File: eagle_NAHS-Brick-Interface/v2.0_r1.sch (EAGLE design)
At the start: 8 parts, among them IC1 FT232RL, J1 NAHS-BRICK-INTERFACE-V2_I-SIDE, J2 10118194-0001LF

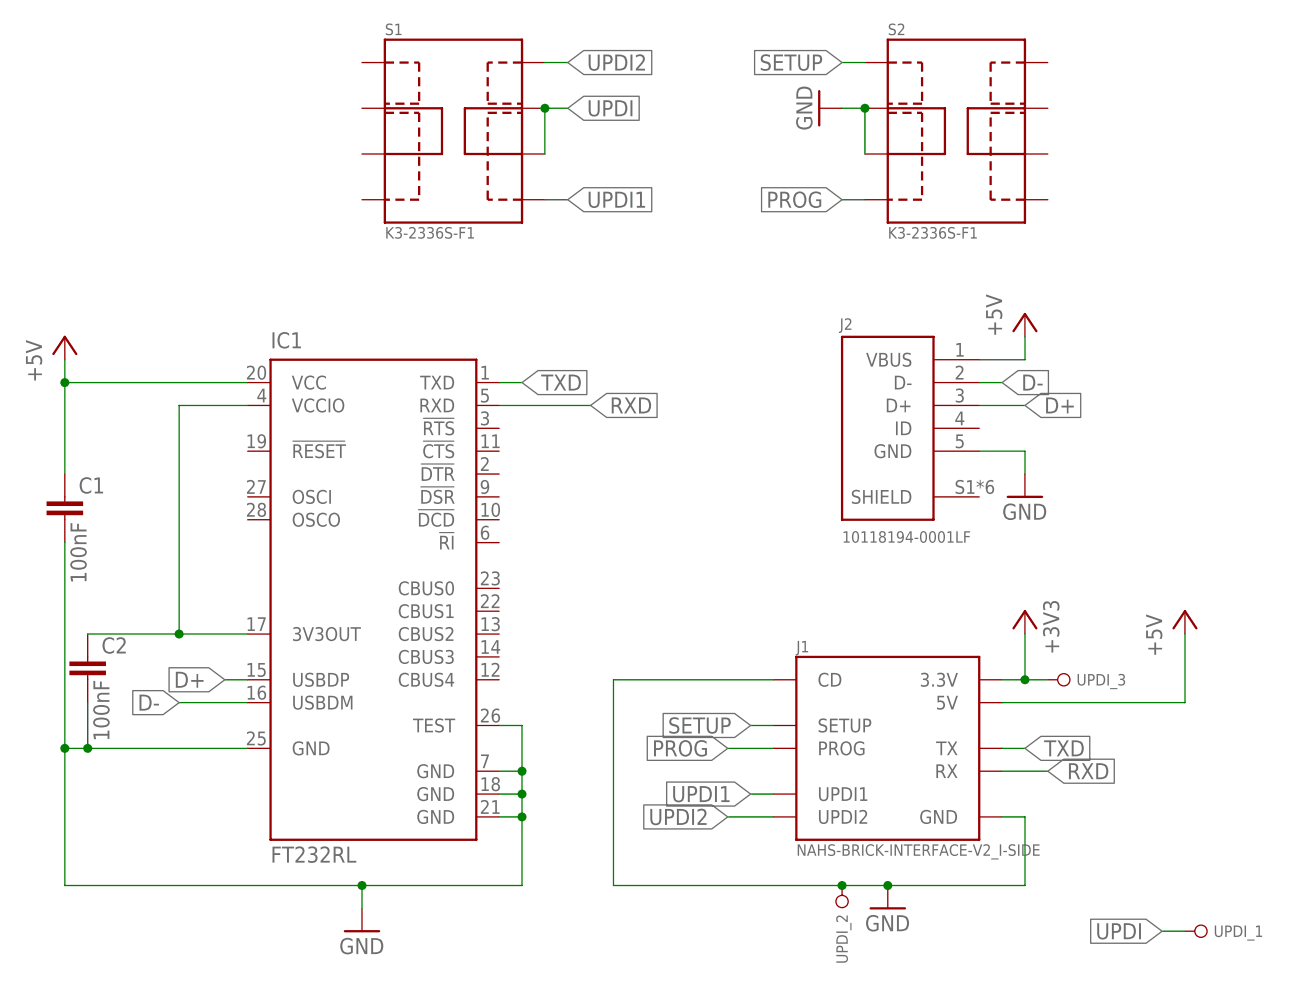
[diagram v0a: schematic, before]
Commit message: added third UPDI Pin
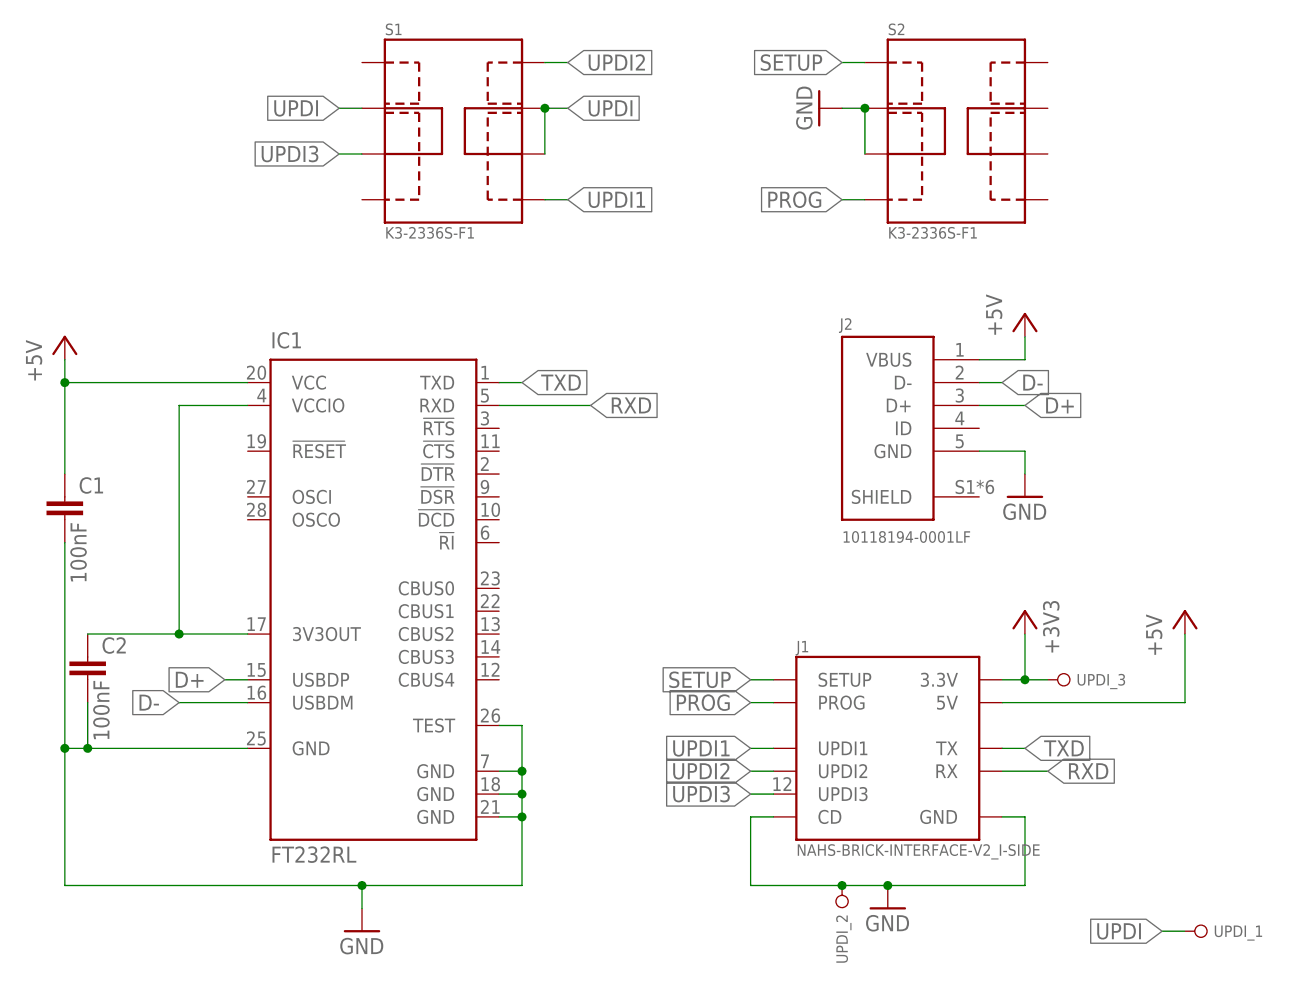
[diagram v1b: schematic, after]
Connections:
- new net UPDI3: J1.UPDI3, S1.1.3
- net UPDI: now also S1.1.2
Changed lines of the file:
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@@
 <pinref part="J1" gate="G$1" pin="GND"/>
 <wire x1="109.22" y1="12.7" x2="106.68" y2="12.7" width="0.1524" layer="91"/>
-<wire x1="88.9" y1="5.08" x2="63.5" y2="5.08" width="0.1524" layer="91"/>
-<wire x1="63.5" y1="5.08" x2="63.5" y2="27.94" width="0.1524" layer="91"/>
+<wire x1="88.9" y1="5.08" x2="78.74" y2="5.08" width="0.1524" layer="91"/>
+<wire x1="78.74" y1="5.08" x2="78.74" y2="12.7" width="0.1524" layer="91"/>
 <junction x="88.9" y="5.08"/>
 <pinref part="J1" gate="G$1" pin="CD"/>
-<wire x1="63.5" y1="27.94" x2="81.28" y2="27.94" width="0.1524" layer="91"/>
+<wire x1="78.74" y1="12.7" x2="81.28" y2="12.7" width="0.1524" layer="91"/>
 </segment>
 <segment>
@@
 <segment>
 <pinref part="J1" gate="G$1" pin="PROG"/>
-<wire x1="81.28" y1="20.32" x2="76.2" y2="20.32" width="0.1524" layer="91"/>
-<label x="76.2" y="20.32" size="1.778" layer="95" rot="R180" xref="yes"/>
+<wire x1="81.28" y1="25.4" x2="78.74" y2="25.4" width="0.1524" layer="91"/>
+<label x="78.74" y="25.4" size="1.778" layer="95" rot="R180" xref="yes"/>
 </segment>
 </net>
@@
 <segment>
 <pinref part="J1" gate="G$1" pin="SETUP"/>
-<wire x1="81.28" y1="22.86" x2="78.74" y2="22.86" width="0.1524" layer="91"/>
-<label x="78.74" y="22.86" size="1.778" layer="95" rot="R180" xref="yes"/>
+<wire x1="81.28" y1="27.94" x2="78.74" y2="27.94" width="0.1524" layer="91"/>
+<label x="78.74" y="27.94" size="1.778" layer="95" rot="R180" xref="yes"/>
 </segment>
 </net>
@@
 <segment>
 <pinref part="J1" gate="G$1" pin="UPDI1"/>
-<wire x1="81.28" y1="15.24" x2="78.74" y2="15.24" width="0.1524" layer="91"/>
-<label x="78.74" y="15.24" size="1.778" layer="95" rot="R180" xref="yes"/>
+<wire x1="81.28" y1="20.32" x2="78.74" y2="20.32" width="0.1524" layer="91"/>
+<label x="78.74" y="20.32" size="1.778" layer="95" rot="R180" xref="yes"/>
 </segment>
 </net>
@@
 <segment>
 <pinref part="J1" gate="G$1" pin="UPDI2"/>
-<wire x1="81.28" y1="12.7" x2="76.2" y2="12.7" width="0.1524" layer="91"/>
-<label x="76.2" y="12.7" size="1.778" layer="95" rot="R180" xref="yes"/>
+<wire x1="81.28" y1="17.78" x2="78.74" y2="17.78" width="0.1524" layer="91"/>
+<label x="78.74" y="17.78" size="1.778" layer="95" rot="R180" xref="yes"/>
 </segment>
 </net>
@@
 <junction x="55.88" y="91.44"/>
 </segment>
+<segment>
+<pinref part="S1" gate="G$1" pin="1.2"/>
+<wire x1="35.56" y1="91.44" x2="33.02" y2="91.44" width="0.1524" layer="91"/>
+<label x="33.02" y="91.44" size="1.778" layer="95" rot="R180" xref="yes"/>
+</segment>
 </net>
 <net name="+3V3" class="0">
@@
 </segment>
 </net>
+<net name="UPDI3" class="0">
+<segment>
+<pinref part="S1" gate="G$1" pin="1.3"/>
+<wire x1="35.56" y1="86.36" x2="33.02" y2="86.36" width="0.1524" layer="91"/>
+<label x="33.02" y="86.36" size="1.778" layer="95" rot="R180" xref="yes"/>
+</segment>
+<segment>
+<pinref part="J1" gate="G$1" pin="UPDI3"/>
+<wire x1="81.28" y1="15.24" x2="78.74" y2="15.24" width="0.1524" layer="91"/>
+<label x="78.74" y="15.24" size="1.778" layer="95" rot="R180" xref="yes"/>
+</segment>
+</net>
